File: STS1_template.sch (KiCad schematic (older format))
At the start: 18 parts, among them IC1 W25Q01JVZEIQ, IC2 CY15B108QN-40SXI, IC3 STM32F411RET6TR, J1 Conn_01x02_Female, J2 Conn_02x16_Odd_Even, J3 Conn_01x02_Female, J4 Conn_02x16_Odd_Even, J5 Conn_02x16_Odd_Even, J6 Conn_02x16_Odd_Even, U1 coordinate_system

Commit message: added Leds and few pin headers
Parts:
- removed J2, J4, J5, J6: Conn_02x16_Odd_Even, Connector_PinHeader_2.00mm:PinHeader_2x16_P2.00mm_Vertical_SMD, symbol Connector_Generic:Conn_02x16_Odd_Even
- added D? (x6): LED, symbol Device:LED
- added J? (x6): Conn_01x01_Male, symbol Connector:Conn_01x01_Male
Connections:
- wire segments 85 -> 102

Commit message: schematic cleanup
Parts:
- removed D? (x6): LED, symbol Device:LED
- removed IC1: W25Q01JVZEIQ, W25Q01JVZEIQ:SON127P800X600X80-9N-D, symbol W25Q01JVZEIQ:W25Q01JVZEIQ
- removed IC2: CY15B108QN-40SXI, CY15B108QN-40SXI:SOIC127P800X203-8N, symbol CY15B108QN-40SXI:CY15B108QN-40SXI
- removed IC3: STM32F411RET6TR, STM32F411RET6TR:QFP50P1200X1200X160-64N, symbol STM32F411RET6TR:STM32F411RET6TR
- removed J1, J3: Conn_01x02_Female, Connector_PinSocket_2.00mm:PinSocket_1x02_P2.00mm_Vertical, symbol Connector:Conn_01x02_Female
- removed J? (x6): Conn_01x01_Male, symbol Connector:Conn_01x01_Male
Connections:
- net labels removed: +3.3V, Earth
- wire segments 102 -> 0

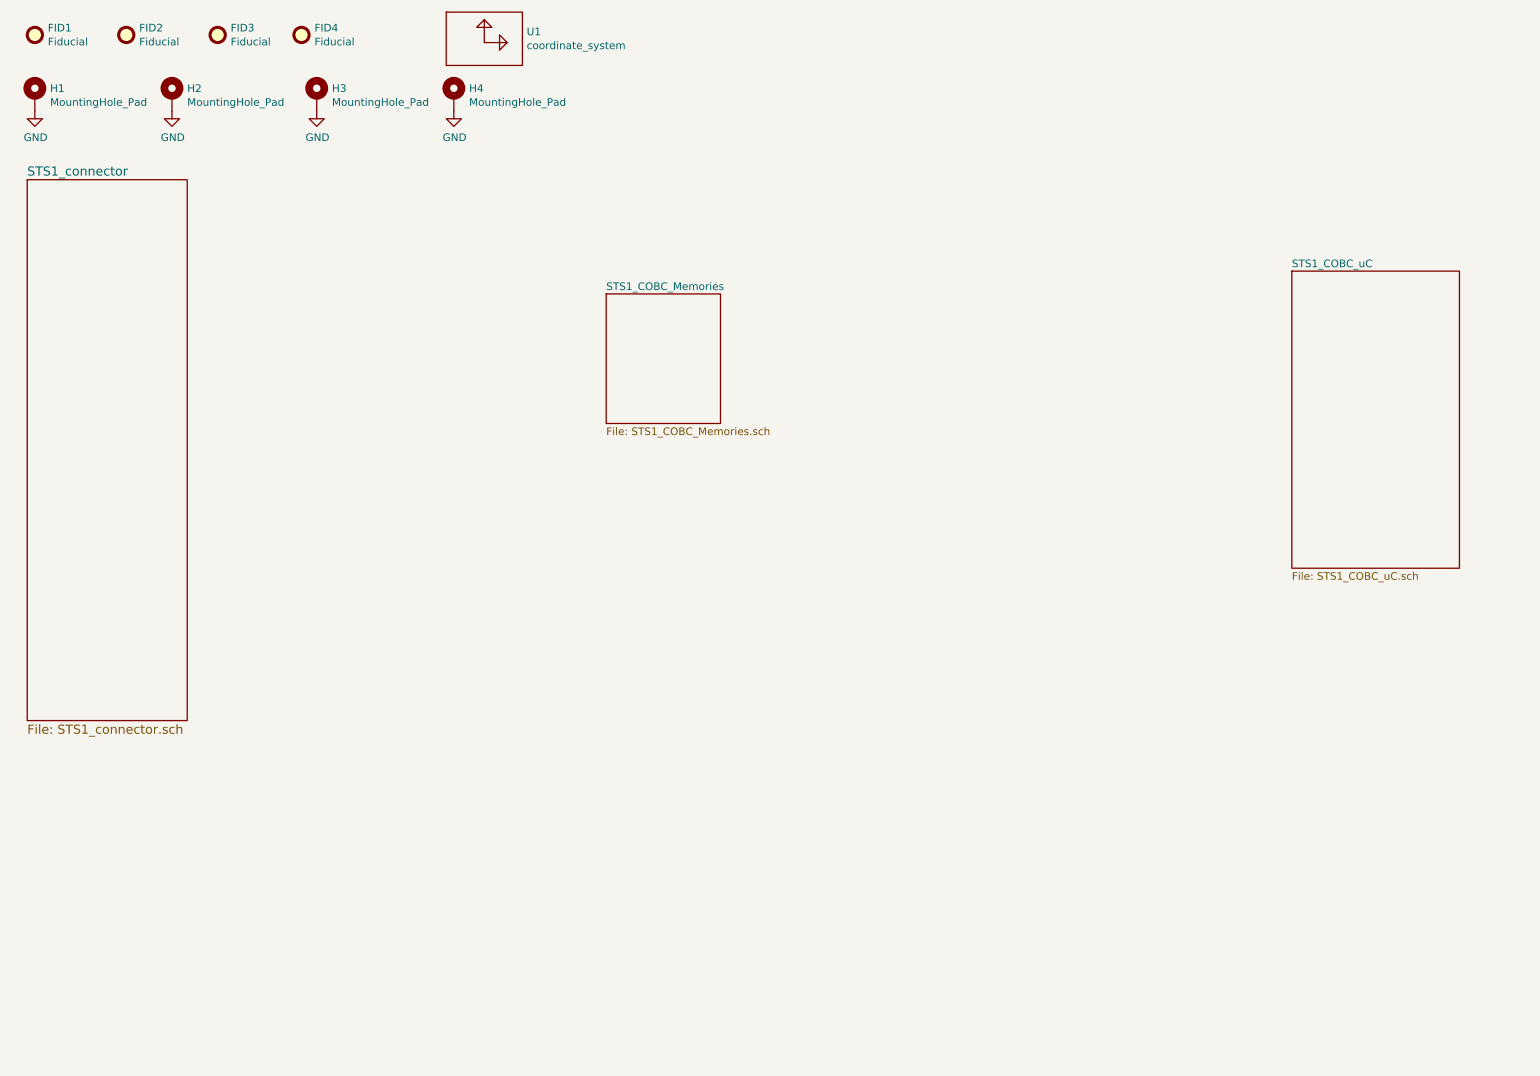
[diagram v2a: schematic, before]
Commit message: RF modules added + some tweaking on STM32
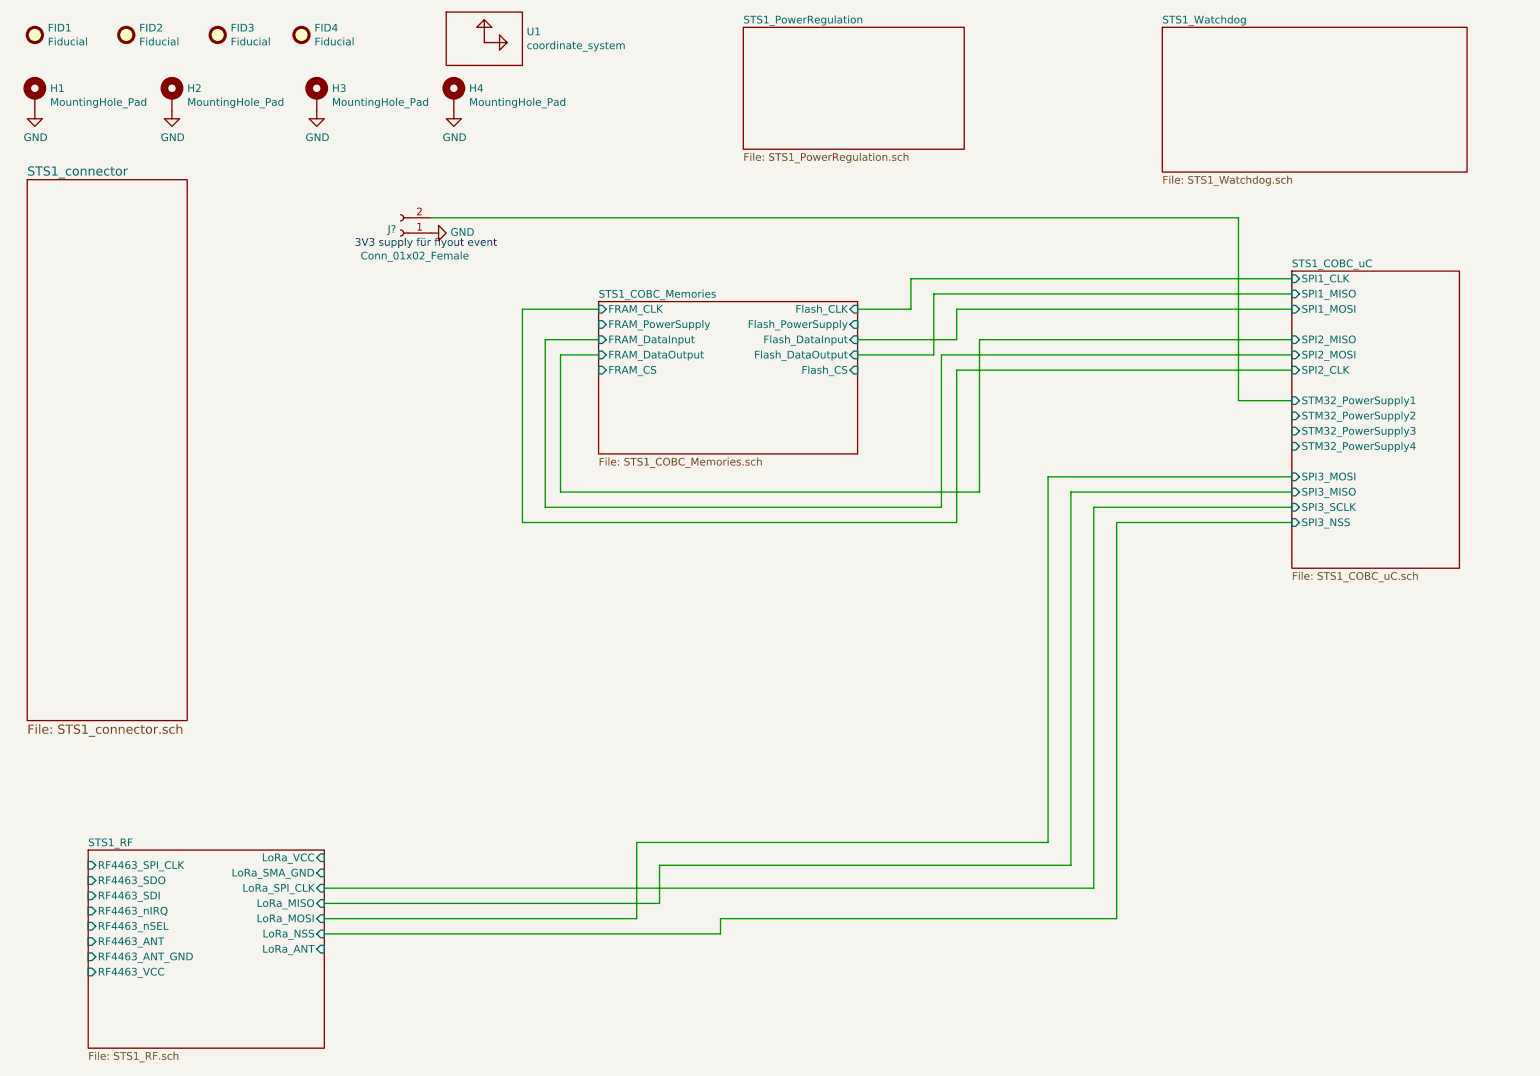
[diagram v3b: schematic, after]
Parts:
- added J?: Conn_01x02_Female, symbol Connector:Conn_01x02_Female
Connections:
- net GND: now also J?.1 (Pin_1)
- new net STS1_COBC_uC/STM32_PowerSupply1: J?.2 (Pin_2)
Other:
- note added: "3V3 supply für flyout event\n"
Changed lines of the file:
@@
 $Descr A4 11693 8268
 encoding utf-8
-Sheet 1 4
+Sheet 1 7
 Title "STS1 COBC HW"
 Date "31.07.2021"
@@
 F0 "STS1_COBC_uC" 50
 F1 "STS1_COBC_uC.sch" 50
-$EndSheet
-$Sheet
-S 4450 2400 750  850
+F2 "SPI1_CLK" I L 8950 2300 50
+F3 "SPI1_MISO" I L 8950 2400 50
+F4 "SPI1_MOSI" I L 8950 2500 50
+F5 "SPI2_MISO" I L 8950 2700 50
+F6 "SPI2_MOSI" I L 8950 2800 50
+F7 "SPI2_CLK" I L 8950 2900 50
+F8 "STM32_PowerSupply1" I L 8950 3100 50
+F9 "STM32_PowerSupply2" I L 8950 3200 50
+F10 "STM32_PowerSupply3" I L 8950 3300 50
+F11 "STM32_PowerSupply4" I L 8950 3400 50
+F12 "SPI3_MOSI" I L 8950 3600 50
+F13 "SPI3_MISO" I L 8950 3700 50
+F14 "SPI3_SCLK" I L 8950 3800 50
+F15 "SPI3_NSS" I L 8950 3900 50
+$EndSheet
+$Sheet
+S 4400 2450 1700 1000
 U 612A52BF
 F0 "STS1_COBC_Memories" 50
 F1 "STS1_COBC_Memories.sch" 50
-$EndSheet
+F2 "Flash_CLK" I R 6100 2500 50
+F3 "Flash_PowerSupply" I R 6100 2600 50
+F4 "Flash_DataInput" I R 6100 2700 50
+F5 "Flash_DataOutput" I R 6100 2800 50
+F6 "Flash_CS" I R 6100 2900 50
+F7 "FRAM_CS" I L 4400 2900 50
+F8 "FRAM_CLK" I L 4400 2500 50
+F9 "FRAM_DataInput" I L 4400 2700 50
+F10 "FRAM_DataOutput" I L 4400 2800 50
+F11 "FRAM_PowerSupply" I L 4400 2600 50
+$EndSheet
+Wire Wire Line
+	8950 2300 6450 2300
+Wire Wire Line
+	6450 2300 6450 2500
+Wire Wire Line
+	6450 2500 6100 2500
+Wire Wire Line
+	8950 2400 6600 2400
+Wire Wire Line
+	6600 2400 6600 2800
+Wire Wire Line
+	6600 2800 6100 2800
+Wire Wire Line
+	8950 2500 6750 2500
+Wire Wire Line
+	6750 2500 6750 2700
+Wire Wire Line
+	6750 2700 6100 2700
+Wire Wire Line
+	8950 2900 6750 2900
+Wire Wire Line
+	6750 2900 6750 3900
+Wire Wire Line
+	6750 3900 3900 3900
+Wire Wire Line
+	3900 3900 3900 2500
+Wire Wire Line
+	3900 2500 4400 2500
+Wire Wire Line
+	8950 2800 6650 2800
+Wire Wire Line
+	6650 2800 6650 3800
+Wire Wire Line
+	6650 3800 4050 3800
+Wire Wire Line
+	4050 3800 4050 2700
+Wire Wire Line
+	4050 2700 4400 2700
+Wire Wire Line
+	8950 2700 6900 2700
+Wire Wire Line
+	6900 2700 6900 3700
+Wire Wire Line
+	6900 3700 4150 3700
+Wire Wire Line
+	4150 3700 4150 2800
+Wire Wire Line
+	4150 2800 4400 2800
+$Sheet
+S 5350 650  1450 800
+U 61293CFB
+F0 "STS1_PowerRegulation" 50
+F1 "STS1_PowerRegulation.sch" 50
+$EndSheet
+$Sheet
+S 8100 650  2000 950
+U 612B4A25
+F0 "STS1_Watchdog" 50
+F1 "STS1_Watchdog.sch" 50
+$EndSheet
+$Comp
+L Connector:Conn_01x02_Female J?
+U 1 1 612F969D
+P 3100 2000
+F 0 "J?" H 3128 1976 50  0000 L CNN
+F 1 "Conn_01x02_Female" H 2650 2150 50  0000 L CNN
+F 2 "" H 3100 2000 50  0001 C CNN
+F 3 "~" H 3100 2000 50  0001 C CNN
+	1    3100 2000
+	-1   0    0    1
+$EndComp
+Text Notes 2800 2100 0    50   ~ 0
+3V3 supply für flyout event\n
+Wire Wire Line
+	3300 1900 8600 1900
+Wire Wire Line
+	8600 1900 8600 3100
+Wire Wire Line
+	8600 3100 8950 3100
+$Comp
+L power:GND #PWR?
+U 1 1 612FF8A3
+P 3300 2000
+F 0 "#PWR?" H 3300 1750 50  0001 C CNN
+F 1 "GND" V 3305 1872 50  0000 R CNN
+F 2 "" H 3300 2000 50  0001 C CNN
+F 3 "" H 3300 2000 50  0001 C CNN
+	1    3300 2000
+	0    -1   -1   0
+$EndComp
+$Sheet
+S 1050 6050 1550 1300
+U 6127F98A
+F0 "STS1_RF" 50
+F1 "STS1_RF.sch" 50
+F2 "LoRa_VCC" I R 2600 6100 50
+F3 "LoRa_SMA_GND" I R 2600 6200 50
+F4 "LoRa_SPI_CLK" I R 2600 6300 50
+F5 "LoRa_MISO" I R 2600 6400 50
+F6 "LoRa_MOSI" I R 2600 6500 50
+F7 "LoRa_NSS" I R 2600 6600 50
+F8 "RF4463_VCC" I L 1050 6850 50
+F9 "RF4463_ANT_GND" I L 1050 6750 50
+F10 "RF4463_ANT" I L 1050 6650 50
+F11 "RF4463_nSEL" I L 1050 6550 50
+F12 "RF4463_nIRQ" I L 1050 6450 50
+F13 "RF4463_SDI" I L 1050 6350 50
+F14 "RF4463_SDO" I L 1050 6250 50
+F15 "RF4463_SPI_CLK" I L 1050 6150 50
+F16 "LoRa_ANT" I R 2600 6700 50
+$EndSheet
+Wire Wire Line
+	8950 3900 7800 3900
+Wire Wire Line
+	7800 3900 7800 6500
+Wire Wire Line
+	5200 6600 5200 6500
+Wire Wire Line
+	5200 6500 7800 6500
+Wire Wire Line
+	5200 6600 2600 6600
+Wire Wire Line
+	8950 3800 7650 3800
+Wire Wire Line
+	7650 3800 7650 6300
+Wire Wire Line
+	7650 6300 2600 6300
+Wire Wire Line
+	7500 3700 7500 6150
+Wire Wire Line
+	7500 6150 4800 6150
+Wire Wire Line
+	4800 6150 4800 6400
+Wire Wire Line
+	4800 6400 2600 6400
+Wire Wire Line
+	7500 3700 8950 3700
+Wire Wire Line
+	7350 3600 7350 6000
+Wire Wire Line
+	7350 6000 4650 6000
+Wire Wire Line
+	4650 6000 4650 6500
+Wire Wire Line
+	2600 6500 4650 6500
+Wire Wire Line
+	7350 3600 8950 3600
 $EndSCHEMATC

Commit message: finished schematic
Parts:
- gave numbers to parts that had none: 1
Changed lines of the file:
@@
 F14 "SPI3_SCLK" I L 8950 3800 50
 F15 "SPI3_NSS" I L 8950 3900 50
+F16 "SPI4_MOSI" I R 10050 3600 50
+F17 "SPI4_MISO" I R 10050 3700 50
+F18 "SPI2_NSS" I L 8950 2600 50
+F19 "SPI4_NSS" I R 10050 3800 50
+F20 "SPI4_SCLK" I R 10050 3900 50
+F21 "STM32_NRST" I R 10050 2300 50
+F22 "STM32_PA9(Watchdog_toggle)" I R 10050 3000 50
 $EndSheet
 $Sheet
@@
 F0 "STS1_Watchdog" 50
 F1 "STS1_Watchdog.sch" 50
+F2 "Watchdog_VCC" I L 8100 1150 50
+F3 "Watchdog_DO(RST)" I R 10100 1250 50
+F4 "Watchdog_DI" I R 10100 1050 50
 $EndSheet
 $Comp
-L Connector:Conn_01x02_Female J?
+L Connector:Conn_01x02_Female J1
 U 1 1 612F969D
 P 3100 2000
-F 0 "J?" H 3128 1976 50  0000 L CNN
+F 0 "J1" H 3128 1976 50  0000 L CNN
 F 1 "Conn_01x02_Female" H 2650 2150 50  0000 L CNN
 F 2 "" H 3100 2000 50  0001 C CNN
@@
 3V3 supply für flyout event\n
 Wire Wire Line
-	3300 1900 8600 1900
+	3300 1900 3900 1900
 Wire Wire Line
 	8600 1900 8600 3100
@@
 	8600 3100 8950 3100
 $Comp
-L power:GND #PWR?
+L power:GND #PWR0123
 U 1 1 612FF8A3
 P 3300 2000
-F 0 "#PWR?" H 3300 1750 50  0001 C CNN
+F 0 "#PWR0123" H 3300 1750 50  0001 C CNN
 F 1 "GND" V 3305 1872 50  0000 R CNN
 F 2 "" H 3300 2000 50  0001 C CNN
@@
 Wire Wire Line
 	7350 3600 8950 3600
+Wire Wire Line
+	3900 1900 3900 2400
+Wire Wire Line
+	3900 2400 3750 2400
+Wire Wire Line
+	3750 2400 3750 5900
+Wire Wire Line
+	3750 6100 2600 6100
+Connection ~ 3900 1900
+Wire Wire Line
+	3900 1900 7650 1900
+Wire Wire Line
+	3750 5900 550  5900
+Wire Wire Line
+	550  5900 550  6850
+Wire Wire Line
+	550  6850 1050 6850
+Connection ~ 3750 5900
+Wire Wire Line
+	3750 5900 3750 6100
+Wire Wire Line
+	8600 3100 8600 3200
+Wire Wire Line
+	8600 3200 8950 3200
+Connection ~ 8600 3100
+Wire Wire Line
+	8600 3200 8600 3300
+Wire Wire Line
+	8600 3300 8950 3300
+Connection ~ 8600 3200
+Wire Wire Line
+	8600 3300 8600 3400
+Wire Wire Line
+	8600 3400 8950 3400
+Connection ~ 8600 3300
+Wire Wire Line
+	10050 3900 10200 3900
+Wire Wire Line
+	10200 3900 10200 5800
+Wire Wire Line
+	10200 5800 650  5800
+Wire Wire Line
+	650  5800 650  6150
+Wire Wire Line
+	650  6150 1050 6150
+Wire Wire Line
+	10050 3800 10300 3800
+Wire Wire Line
+	10300 3800 10300 5700
+Wire Wire Line
+	10300 5700 750  5700
+Wire Wire Line
+	750  5700 750  6550
+Wire Wire Line
+	750  6550 1050 6550
+Wire Wire Line
+	10050 3700 10400 3700
+Wire Wire Line
+	10400 3700 10400 5600
+Wire Wire Line
+	10400 5600 850  5600
+Wire Wire Line
+	850  5600 850  6250
+Wire Wire Line
+	850  6250 1050 6250
+Wire Wire Line
+	10050 3600 10500 3600
+Wire Wire Line
+	10500 3600 10500 5500
+Wire Wire Line
+	10500 5500 950  5500
+Wire Wire Line
+	950  5500 950  6350
+Wire Wire Line
+	950  6350 1050 6350
+Wire Wire Line
+	8950 2600 7000 2600
+Wire Wire Line
+	7000 2600 7000 3600
+Wire Wire Line
+	7000 3600 4250 3600
+Wire Wire Line
+	4250 3600 4250 2900
+Wire Wire Line
+	4250 2900 4400 2900
+Wire Wire Line
+	7650 1900 7650 1150
+Wire Wire Line
+	7650 1150 8100 1150
+Connection ~ 7650 1900
+Wire Wire Line
+	7650 1900 8600 1900
+Wire Wire Line
+	10100 1250 10500 1250
+Wire Wire Line
+	10500 1250 10500 2300
+Wire Wire Line
+	10500 2300 10050 2300
+Wire Wire Line
+	10050 3000 10400 3000
+Wire Wire Line
+	10400 3000 10400 1050
+Wire Wire Line
+	10400 1050 10100 1050
 $EndSCHEMATC

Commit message: new template
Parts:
- J1: footprint (none) -> Connector_PinHeader_2.54mm:PinHeader_1x02_P2.54mm_Vertical
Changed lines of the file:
@@
 F 0 "J1" H 3128 1976 50  0000 L CNN
 F 1 "Conn_01x02_Female" H 2650 2150 50  0000 L CNN
-F 2 "" H 3100 2000 50  0001 C CNN
+F 2 "Connector_PinHeader_2.54mm:PinHeader_1x02_P2.54mm_Vertical" H 3100 2000 50  0001 C CNN
 F 3 "~" H 3100 2000 50  0001 C CNN
 	1    3100 2000
